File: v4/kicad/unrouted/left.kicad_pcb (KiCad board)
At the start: 2 copper layers, 160 x 118.6 mm, 67 parts

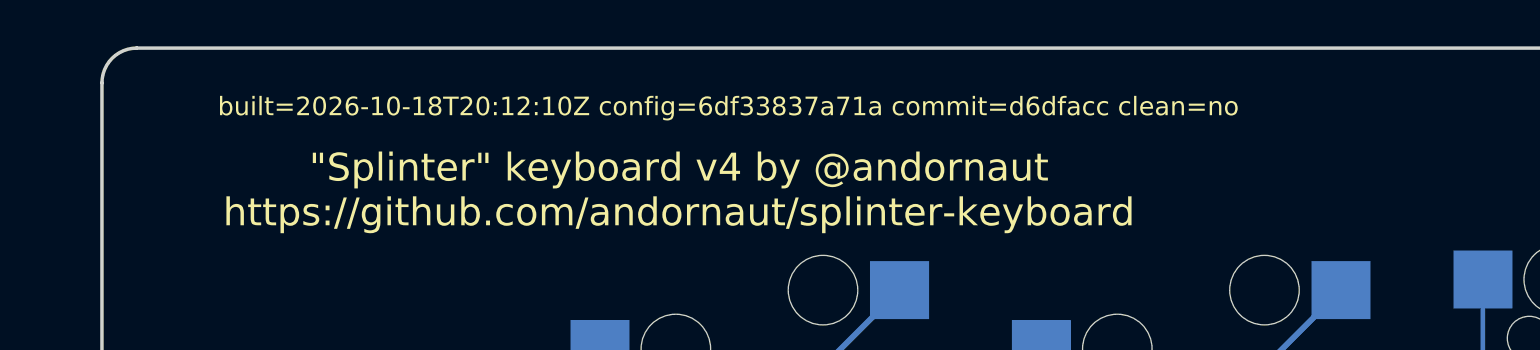
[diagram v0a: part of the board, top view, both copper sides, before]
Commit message: Rebuild the v4 boards from config 6df33837a71a
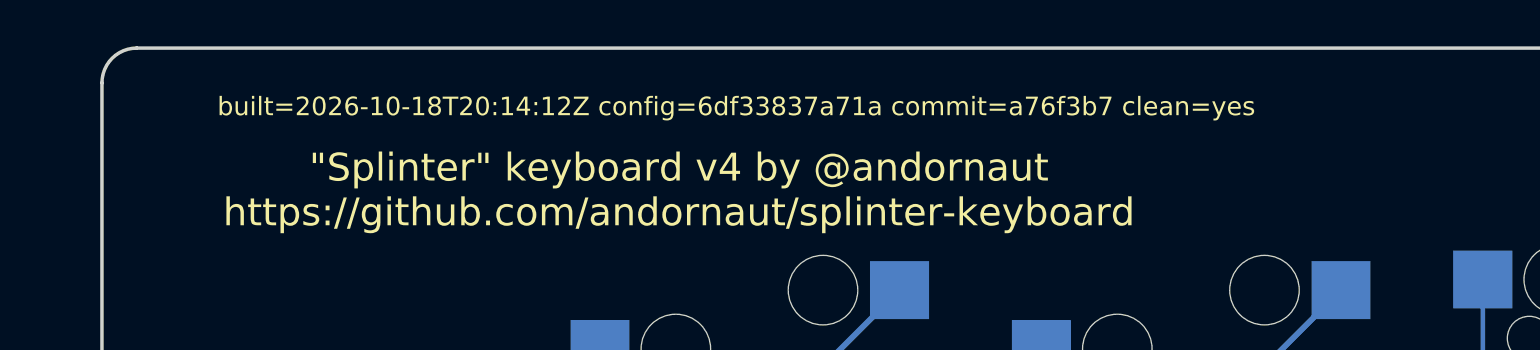
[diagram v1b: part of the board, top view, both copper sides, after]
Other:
- board text added: "built=2026-10-18T20:14:12Z config=6df33837a71a commit=a76f3b7 clean=yes"
- board text removed: "built=2026-10-18T20:12:10Z config=6df33837a71a commit=d6dfacc clean=no"

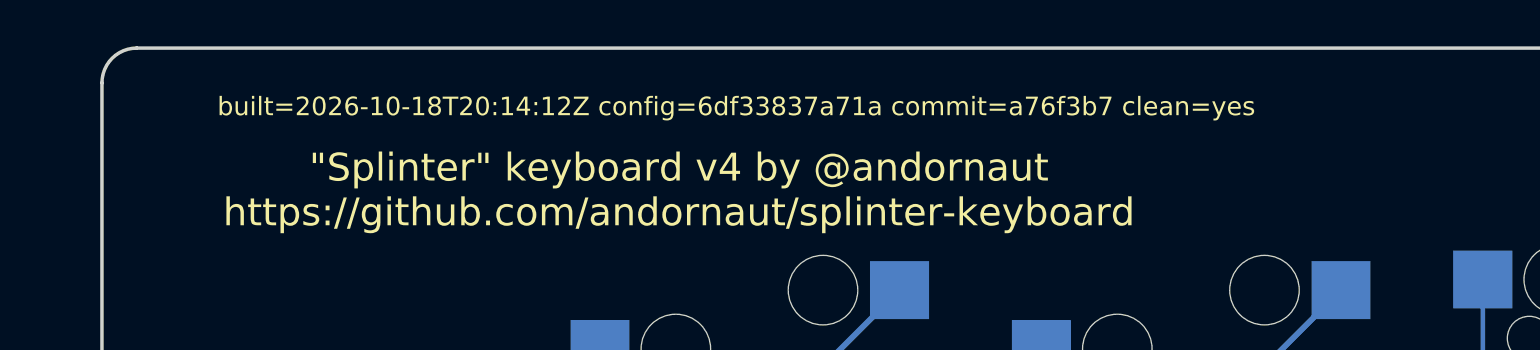
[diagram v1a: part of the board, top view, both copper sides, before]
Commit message: Keep copper out from under the v4 reset switch frame
Add a back-copper rule area between each side's two reset-switch pads, the
prohibited area for copper tracks on ALPS's SKQG land drawing. It disallows
pour, tracks and vias on the switch's own layer only, so the F.Cu matrix
traces under the switch stay. add-keepout-zones.py maps the area from the
footprint frame through the switch's own pads, so it follows the part on both
halves.
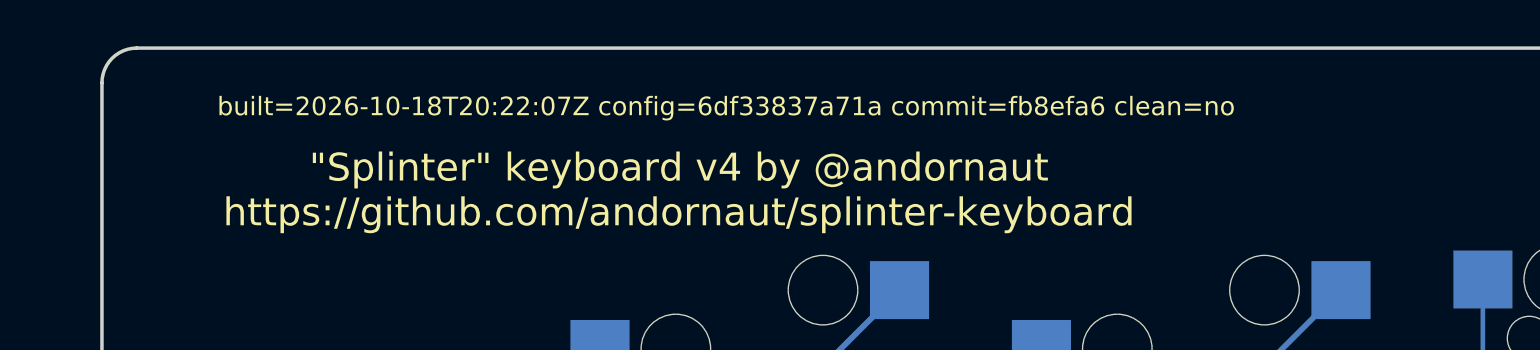
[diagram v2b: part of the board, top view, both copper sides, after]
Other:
- board text added: "built=2026-10-18T20:22:07Z config=6df33837a71a commit=fb8efa6 clean=no"
- board text removed: "built=2026-10-18T20:14:12Z config=6df33837a71a commit=a76f3b7 clean=yes"

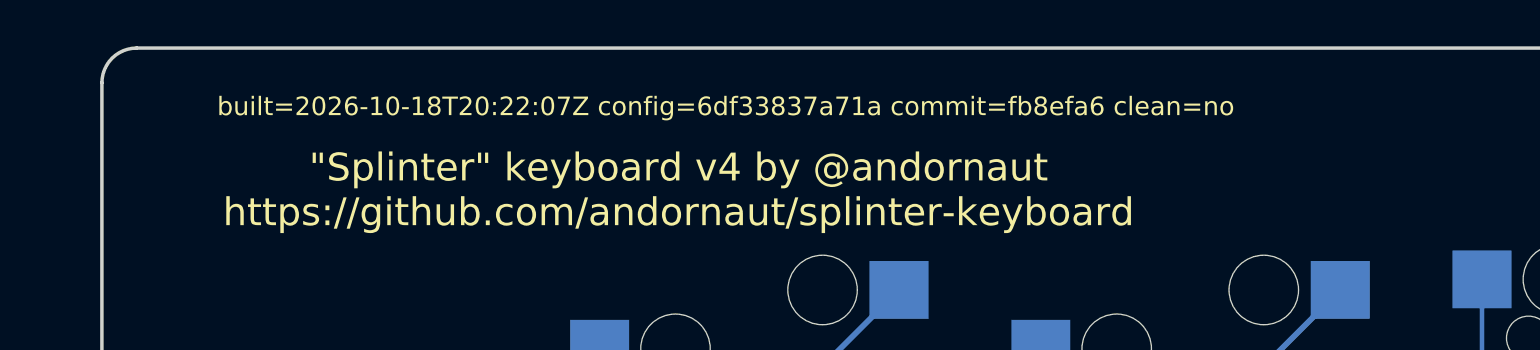
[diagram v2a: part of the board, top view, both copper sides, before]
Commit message: Rebuild the v4 boards from config 6df33837a71a
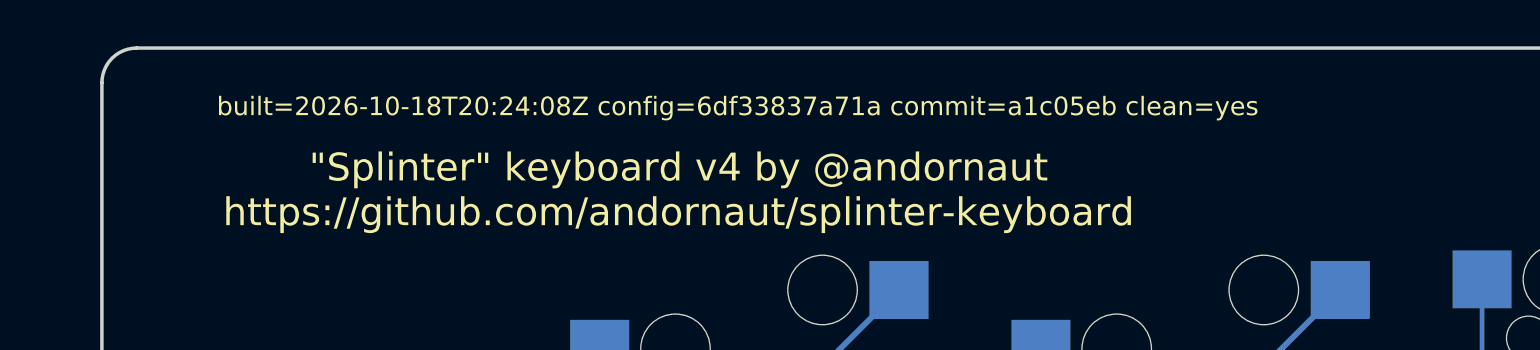
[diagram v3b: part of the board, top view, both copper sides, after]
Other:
- board text added: "built=2026-10-18T20:24:08Z config=6df33837a71a commit=a1c05eb clean=yes"
- board text removed: "built=2026-10-18T20:22:07Z config=6df33837a71a commit=fb8efa6 clean=no"

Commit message: Clear the pour around the v4 reset switch, and correct the order docs
- Add a pour-only rule area around each reset switch and its four pads, so
  the GND pour leaves a clean rectangle there. Tracks stay allowed: the
  switch's own GND and RST traces run along its pad rows.
- JLCCNC: annotate the overall cavity (161.00 x 119.59) and plate
  (160.60 x 119.14) sizes, which are what the parts measure; give the shell
  and plate order remarks; the shell PDFs carry only the thread callouts.
- State the 3.6V jumper hazard for the case where the half with USB is
  still at 5V.
- BUILD.md: the board's pocket play is 0.48-0.50 per side.
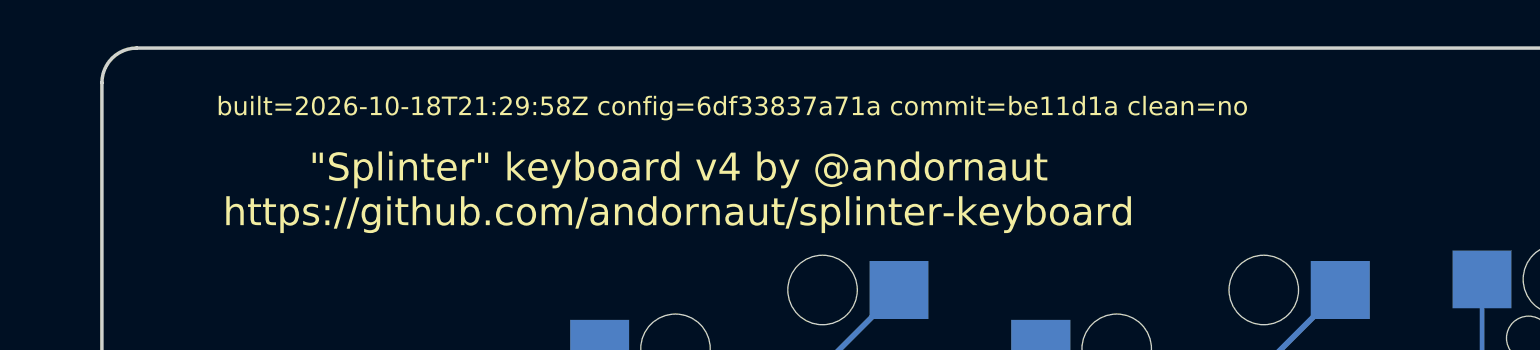
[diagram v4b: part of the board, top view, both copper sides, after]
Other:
- board text added: "built=2026-10-18T21:29:58Z config=6df33837a71a commit=be11d1a clean=no"
- board text removed: "built=2026-10-18T20:24:08Z config=6df33837a71a commit=a1c05eb clean=yes"

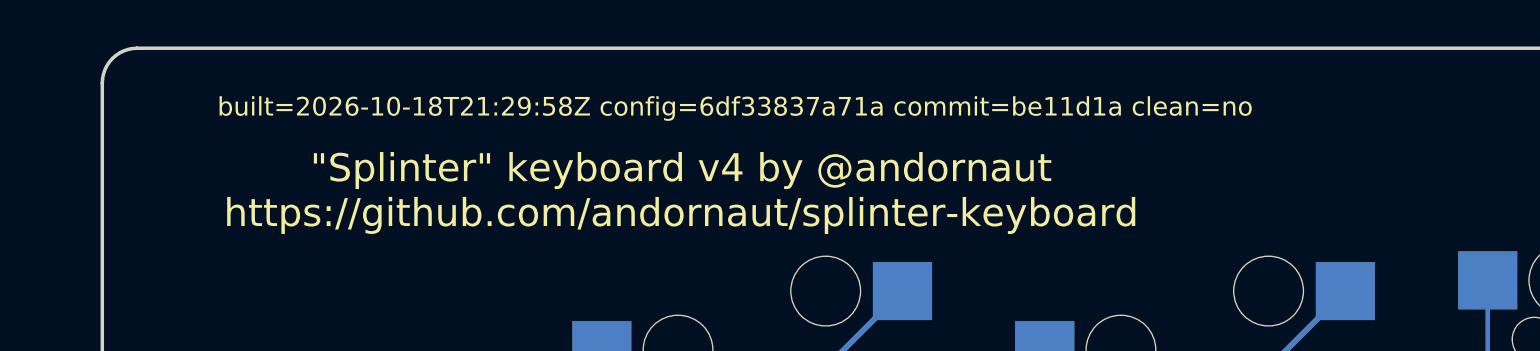
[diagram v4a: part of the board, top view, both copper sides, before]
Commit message: Rebuild the v4 boards from config 6df33837a71a
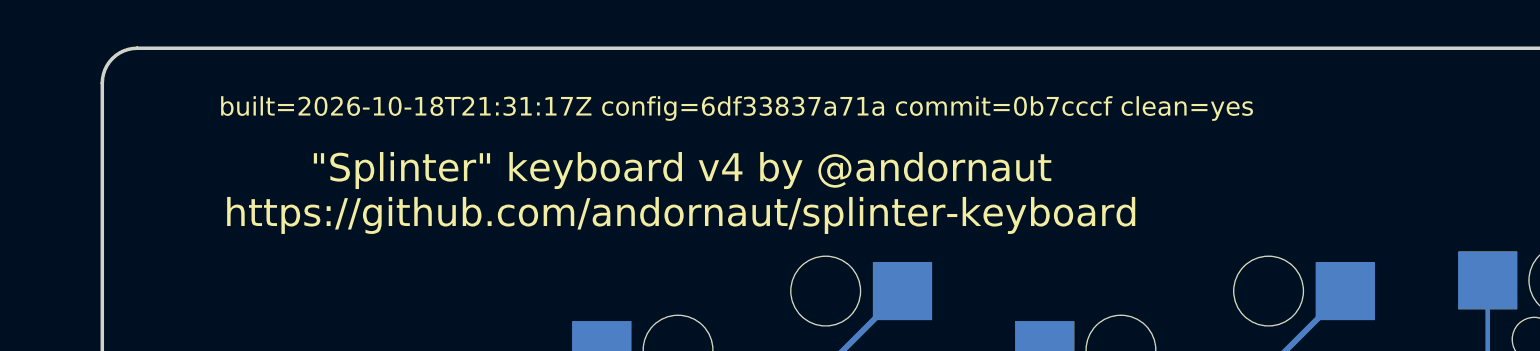
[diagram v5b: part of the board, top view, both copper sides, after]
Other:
- board text added: "built=2026-10-18T21:31:17Z config=6df33837a71a commit=0b7cccf clean=yes"
- board text removed: "built=2026-10-18T21:29:58Z config=6df33837a71a commit=be11d1a clean=no"

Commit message: Rebuild the v4 boards from config 6df33837a71a
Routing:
- net P9: track 138.1 -> 130.9 mm
- net P8: track 166.3 -> 159.1 mm
- net P10: track 226.9 -> 219.7 mm
- net P7: track 192.0 -> 184.8 mm
- net P5: track 130.3 -> 123.1 mm
- net five_mod: track 12.0 -> 10.8 mm, vias 1 -> 0
- net zero_upper: track 13.7 -> 12.5 mm, vias 1 -> 0
- net zero_mod: track 13.7 -> 12.5 mm, vias 1 -> 0
- net zero_lower: track 13.7 -> 12.5 mm, vias 1 -> 0
- net zero_home: track 13.7 -> 12.5 mm, vias 1 -> 0
- net three_mod: track 12.0 -> 10.8 mm, vias 1 -> 0
- net one_upper: track 13.7 -> 12.5 mm, vias 1 -> 0
- net one_num: track 13.7 -> 12.5 mm, vias 1 -> 0
- net one_mod: track 13.7 -> 12.5 mm, vias 1 -> 0
- net one_lower: track 13.7 -> 12.5 mm, vias 1 -> 0
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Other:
- board text added: "built=2026-10-18T21:37:48Z config=6df33837a71a commit=0faebac clean=yes"
- board text removed: "built=2026-10-18T21:31:17Z config=6df33837a71a commit=0b7cccf clean=yes"

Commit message: Rebuild the v4 boards from config 6df33837a71a
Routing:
- net P10: track 219.7 -> 226.9 mm
- net P8: track 159.1 -> 166.3 mm
- net P9: track 130.9 -> 138.1 mm
- net P7: track 184.8 -> 192.0 mm
- net P5: track 123.1 -> 130.3 mm
- net five_mod: track 10.8 -> 12.0 mm, vias 0 -> 1
- net zero_upper: track 12.5 -> 13.7 mm, vias 0 -> 1
- net zero_mod: track 12.5 -> 13.7 mm, vias 0 -> 1
- net zero_lower: track 12.5 -> 13.7 mm, vias 0 -> 1
- net zero_home: track 12.5 -> 13.7 mm, vias 0 -> 1
- net three_mod: track 10.8 -> 12.0 mm, vias 0 -> 1
- net one_upper: track 12.5 -> 13.7 mm, vias 0 -> 1
- net one_num: track 12.5 -> 13.7 mm, vias 0 -> 1
- net one_mod: track 12.5 -> 13.7 mm, vias 0 -> 1
- net one_lower: track 12.5 -> 13.7 mm, vias 0 -> 1
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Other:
- board text added: "built=2026-10-18T22:24:53Z config=6df33837a71a commit=84199d1 clean=yes"
- board text removed: "built=2026-10-18T21:37:48Z config=6df33837a71a commit=0faebac clean=yes"

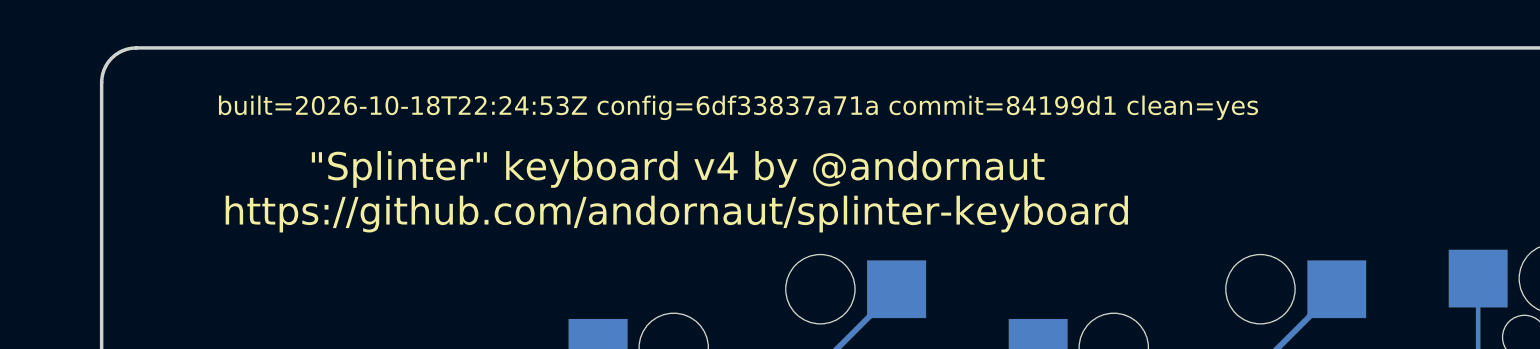
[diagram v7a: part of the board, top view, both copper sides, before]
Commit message: Rebuild the v4 boards from config 6df33837a71a
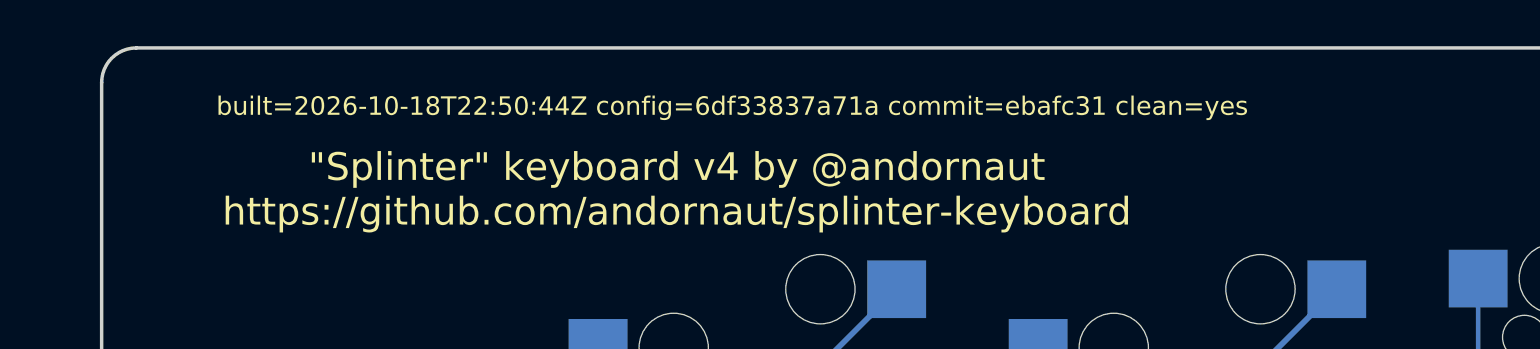
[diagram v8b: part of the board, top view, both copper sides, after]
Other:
- board text added: "built=2026-10-18T22:50:44Z config=6df33837a71a commit=ebafc31 clean=yes"
- board text removed: "built=2026-10-18T22:24:53Z config=6df33837a71a commit=84199d1 clean=yes"
